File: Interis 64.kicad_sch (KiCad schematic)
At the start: 11 parts, among them J2 Ext. RESET, SW1 RESET, U1 DS1233, U2 Z80B CPU, Y1 7.3728MHz

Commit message: Memory expansion moved to low memory
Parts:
- J2: footprint Connector_PinHeader_2.54mm:PinHeader_1x02_P2.54mm_Vertical -> Connector_JST:JST_XH_B2B-XH-A_1x02_P2.50mm_Vertical
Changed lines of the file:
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@@
       (effects (font (size 1.27 1.27)) (justify left))
     )
-    (property "Footprint" "Connector_PinHeader_2.54mm:PinHeader_1x02_P2.54mm_Vertical" (at 111.125 41.91 0)
+    (property "Footprint" "Connector_JST:JST_XH_B2B-XH-A_1x02_P2.50mm_Vertical" (at 111.125 41.91 0)
       (effects (font (size 1.27 1.27)) hide)
     )

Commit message: Misc Updates/Cleanup
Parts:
- C29: value 0.01µF -> 0.1µF; footprint Capacitor_THT:C_Disc_D3.8mm_W2.6mm_P2.50mm -> Capacitor_THT:C_Disc_D5.0mm_W2.5mm_P2.50mm
- TP1, TP2: footprint TestPoint:TestPoint_THTPad_2.5x2.5mm_Drill1.2mm -> TestPoint:TestPoint_Loop_D2.60mm_Drill1.6mm_Beaded
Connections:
- net ~{RFSH}: now reaches U2.28 (~{RFSH})
- no-connect marks 2 -> 1
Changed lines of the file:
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@@
   )
   (no_connect (at 63.5 76.835))
-  (no_connect (at 133.35 112.395))
   (bus_entry (at 173.99 112.395) (size 2.54 -2.54)
     (stroke (width 0) (type default))
@@
   )
   (wire (pts (xy 127 38.1) (xy 127 84.455))
+    (stroke (width 0) (type default))
+  )
+  (wire (pts (xy 125.73 112.395) (xy 133.35 112.395))
     (stroke (width 0) (type default))
   )
@@
     (effects (font (size 1.27 1.27)) (justify right))
     (property "Intersheetrefs" "${INTERSHEET_REFS}" (at 86.2734 114.8556 0)
+      (effects (font (size 1.27 1.27)) (justify right) hide)
+    )
+  )
+  (global_label "~{RFSH}" (shape output) (at 125.73 112.395 180) (fields_autoplaced)
+    (effects (font (size 1.27 1.27)) (justify right))
+    (property "Intersheetrefs" "${INTERSHEET_REFS}" (at 118.1034 112.395 0)
       (effects (font (size 1.27 1.27)) (justify right) hide)
     )
@@
       (effects (font (size 1.27 1.27)) (justify right))
     )
-    (property "Value" "0.01µF" (at 80.645 44.45 0)
+    (property "Value" "0.1µF" (at 80.645 44.45 0)
       (effects (font (size 1.27 1.27)) (justify right))
     )
-    (property "Footprint" "Capacitor_THT:C_Disc_D3.8mm_W2.6mm_P2.50mm" (at 89.2048 46.99 0)
+    (property "Footprint" "Capacitor_THT:C_Disc_D5.0mm_W2.5mm_P2.50mm" (at 89.2048 46.99 0)
       (effects (font (size 1.27 1.27)) hide)
     )
@@
       (effects (font (size 1.27 1.27)) (justify right))
     )
-    (property "Footprint" "TestPoint:TestPoint_THTPad_2.5x2.5mm_Drill1.2mm" (at 121.92 33.02 0)
+    (property "Footprint" "TestPoint:TestPoint_Loop_D2.60mm_Drill1.6mm_Beaded" (at 121.92 33.02 0)
       (effects (font (size 1.27 1.27)) hide)
     )
@@
       (effects (font (size 1.27 1.27)))
     )
-    (property "Footprint" "TestPoint:TestPoint_THTPad_2.5x2.5mm_Drill1.2mm" (at 103.505 64.135 0)
-      (effects (font (size 1.27 1.27)) hide)
-    )
+    (property "Footprint" "TestPoint:TestPoint_Loop_D2.60mm_Drill1.6mm_Beaded" (at 103.505 64.135 0)
+      (effects (font (size 1.27 1.27)) hide)
+    )

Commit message: Work-in-progress
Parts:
- removed J2: Ext. RESET, Connector_JST:JST_XH_B2B-XH-A_1x02_P2.50mm_Vertical, symbol Connector_Generic:Conn_01x02
- removed SW1: RESET, Button_Switch_THT:SW_TH_Tactile_Omron_B3F-10xx, symbol Switch:SW_Push
- added J2: ExtReset, Connector_JST:JST_XH_B4B-XH-A_1x04_P2.50mm_Vertical, symbol Connector_Generic:Conn_01x04
- U1: footprint Package_TO_SOT_THT:TO-92_Inline -> Package_TO_SOT_THT:TO-92_HandSolder
- U2: footprint Package_DIP:DIP-40_W15.24mm_LongPads -> Package_DIP:DIP-40_W15.24mm
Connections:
- net +5V: now also J2.1 (Pin_1)
- net GND: now also J2.2 (Pin_2), J2.3 (Pin_3)
- net ~{RESET}: now also J2.4 (Pin_4)
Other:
- removed sheet PS2 Keyboard
- added sheet VT82C42 Input (VT82C42.kicad_sch)
- moved on the sheet: C29, TP2

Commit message: Work in progress
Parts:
- removed TP1: ~{RES}, TestPoint:TestPoint_Loop_D2.60mm_Drill1.6mm_Beaded, symbol Connector:TestPoint
- removed TP2: CLK, TestPoint:TestPoint_Loop_D2.60mm_Drill1.6mm_Beaded, symbol Connector:TestPoint
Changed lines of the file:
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@@
   (junction (at 37.465 135.89) (diameter 0) (color 0 0 0 0)
-  )
-  (junction (at 103.505 69.215) (diameter 0) (color 0 0 0 0)
   )
   (junction (at 97.79 38.1) (diameter 0) (color 0 0 0 0)
@@
   )
   (bus (pts (xy 176.53 130.175) (xy 176.53 132.715))
-    (stroke (width 0) (type default))
-  )
-  (wire (pts (xy 127 33.02) (xy 127 38.1))
     (stroke (width 0) (type default))
   )
@@
     )
   )
-  (symbol (lib_id "Connector:TestPoint") (at 127 33.02 0) (mirror y) (unit 1)
-    (in_bom yes) (on_board yes) (dnp no) (fields_autoplaced)
-    (property "Reference" "TP1" (at 128.397 28.7878 0)
-      (effects (font (size 1.27 1.27)) (justify right))
-    )
-    (property "Value" "~{RES}" (at 128.397 31.4787 0)
-      (effects (font (size 1.27 1.27)) (justify right))
-    )
-    (property "Footprint" "TestPoint:TestPoint_Loop_D2.60mm_Drill1.6mm_Beaded" (at 121.92 33.02 0)
-      (effects (font (size 1.27 1.27)) hide)
-    )
-    (property "Datasheet" "~" (at 121.92 33.02 0)
-      (effects (font (size 1.27 1.27)) hide)
-    )
-    (pin "1")
-    (instances
-      (project "Interis 64"
-        (path "/b7aa0362-7c9e-4a42-b191-ab15a38bf3c5"
-          (reference "TP1") (unit 1)
-        )
-      )
-    )
-  )
   (symbol (lib_id "power:GND") (at 71.12 85.725 0) (unit 1)
     (in_bom yes) (on_board yes) (dnp no)
@@
         )
       )
-    )
-  )
-  (symbol (lib_id "Connector:TestPoint") (at 103.505 69.215 0) (unit 1)
-    (in_bom yes) (on_board yes) (dnp no) (fields_autoplaced)
-    (property "Reference" "TP2" (at 104.902 65.2693 0)
-      (effects (font (size 1.27 1.27)) (justify left))
-    )
-    (property "Value" "CLK" (at 104.902 67.1903 0)
-      (effects (font (size 1.27 1.27)) (justify left))
-    )
-    (property "Footprint" "TestPoint:TestPoint_Loop_D2.60mm_Drill1.6mm_Beaded" (at 108.585 69.215 0)
-      (effects (font (size 1.27 1.27)) hide)
-    )
-    (property "Datasheet" "~" (at 108.585 69.215 0)
-      (effects (font (size 1.27 1.27)) hide)
-    )
-    (pin "1")
-    (instances
-      (project "Interis 64"
-        (path "/b7aa0362-7c9e-4a42-b191-ab15a38bf3c5"
-          (reference "TP2") (unit 1)
-        )
-      )

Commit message: Layout Tweaks
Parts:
- added J1: PwrLED, Connector_PinHeader_2.54mm:PinHeader_1x02_P2.54mm_Vertical, symbol Connector_Generic:Conn_01x02
- J2: footprint Connector_JST:JST_XH_B4B-XH-A_1x04_P2.50mm_Vertical -> Connector_PinHeader_2.54mm:PinHeader_1x02_P2.54mm_Vertical; symbol Connector_Generic:Conn_01x04 -> Connector_Generic:Conn_01x02
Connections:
- net +5V: now also J1.2 (Pin_2); no longer J2.1 (Pin_1)
- net GND: now also J2.1 (Pin_1), J1.1 (Pin_1); no longer J2.2 (Pin_2), J2.3 (Pin_3)
- net ~{RESET}: now also J2.2 (Pin_2); no longer J2.4 (Pin_4)
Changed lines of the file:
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@@
   (junction (at 103.505 99.695) (diameter 0) (color 0 0 0 0)
-  )
-  (junction (at 37.465 135.89) (diameter 0) (color 0 0 0 0)
   )
   (junction (at 97.79 38.1) (diameter 0) (color 0 0 0 0)
@@
     (stroke (width 0) (type default))
   )
+  (wire (pts (xy 48.895 160.02) (xy 52.705 160.02))
+    (stroke (width 0) (type default))
+  )
   (wire (pts (xy 168.91 112.395) (xy 173.99 112.395))
     (stroke (width 0) (type default))
@@
     (stroke (width 0) (type default))
   )
+  (wire (pts (xy 37.465 162.56) (xy 52.705 162.56))
+    (stroke (width 0) (type default))
+  )
   (wire (pts (xy 168.91 140.335) (xy 173.99 140.335))
     (stroke (width 0) (type default))
@@
     (stroke (width 0) (type default))
   )
-  (wire (pts (xy 37.465 135.89) (xy 37.465 144.78))
+  (wire (pts (xy 37.465 133.35) (xy 37.465 144.78))
     (stroke (width 0) (type default))
   )
@@
     (stroke (width 0) (type default))
   )
+  (wire (pts (xy 48.895 156.845) (xy 48.895 160.02))
+    (stroke (width 0) (type default))
+  )
   (wire (pts (xy 168.91 120.015) (xy 173.99 120.015))
     (stroke (width 0) (type default))
@@
     (stroke (width 0) (type default))
   )
-  (wire (pts (xy 37.465 133.35) (xy 37.465 135.89))
-    (stroke (width 0) (type default))
-  )
   (bus (pts (xy 176.53 78.105) (xy 182.88 78.105))
     (stroke (width 0) (type default))
@@
     (stroke (width 0) (type default))
   )
-  (wire (pts (xy 48.895 130.81) (xy 52.705 130.81))
-    (stroke (width 0) (type default))
-  )
   (wire (pts (xy 92.71 142.875) (xy 103.505 142.875))
     (stroke (width 0) (type default))
@@
     (stroke (width 0) (type default))
   )
-  (wire (pts (xy 48.895 127.635) (xy 48.895 130.81))
-    (stroke (width 0) (type default))
-  )
   (bus (pts (xy 176.53 92.075) (xy 176.53 94.615))
     (stroke (width 0) (type default))
@@
     (stroke (width 0) (type default))
   )
+  (wire (pts (xy 37.465 162.56) (xy 37.465 173.99))
+    (stroke (width 0) (type default))
+  )
   (wire (pts (xy 125.73 132.715) (xy 133.35 132.715))
     (stroke (width 0) (type default))
@@
   )
   (bus (pts (xy 176.53 97.155) (xy 176.53 99.695))
-    (stroke (width 0) (type default))
-  )
-  (wire (pts (xy 37.465 135.89) (xy 52.705 135.89))
     (stroke (width 0) (type default))
   )
@@
     )
   )
-  (global_label "~{RESET}" (shape bidirectional) (at 52.705 138.43 180) (fields_autoplaced)
-    (effects (font (size 1.27 1.27)) (justify right))
-    (property "Intersheetrefs" "${INTERSHEET_REFS}" (at 44.6356 138.3506 0)
+  (global_label "~{RESET}" (shape bidirectional) (at 52.705 135.89 180) (fields_autoplaced)
+    (effects (font (size 1.27 1.27)) (justify right))
+    (property "Intersheetrefs" "${INTERSHEET_REFS}" (at 44.6356 135.8106 0)
       (effects (font (size 1.27 1.27)) (justify right) hide)
     )
@@
     )
   )
+  (symbol (lib_id "power:GND") (at 37.465 173.99 0) (unit 1)
+    (in_bom yes) (on_board yes) (dnp no)
+    (property "Reference" "#PWR080" (at 37.465 180.34 0)
+      (effects (font (size 1.27 1.27)) hide)
+    )
+    (property "Value" "GND" (at 37.592 178.3842 0)
+      (effects (font (size 1.27 1.27)))
+    )
+    (property "Footprint" "" (at 37.465 173.99 0)
+      (effects (font (size 1.27 1.27)) hide)
+    )
+    (property "Datasheet" "" (at 37.465 173.99 0)
+      (effects (font (size 1.27 1.27)) hide)
+    )
+    (pin "1")
+    (instances
+      (project "Interis 64"
+        (path "/b7aa0362-7c9e-4a42-b191-ab15a38bf3c5"
+          (reference "#PWR080") (unit 1)
+        )
+      )
+    )
+  )
   (symbol (lib_id "Device:C") (at 97.79 43.18 0) (mirror y) (unit 1)
     (in_bom yes) (on_board yes) (dnp no)
@@
     )
   )
-  (symbol (lib_id "Connector_Generic:Conn_01x04") (at 57.785 133.35 0) (unit 1)
+  (symbol (lib_id "Connector_Generic:Conn_01x02") (at 57.785 133.35 0) (unit 1)
     (in_bom yes) (on_board yes) (dnp no) (fields_autoplaced)
     (property "Reference" "J2" (at 59.817 133.9763 0)
@@
       (effects (font (size 1.27 1.27)) (justify left))
     )
-    (property "Footprint" "Connector_JST:JST_XH_B4B-XH-A_1x04_P2.50mm_Vertical" (at 57.785 133.35 0)
+    (property "Footprint" "Connector_PinHeader_2.54mm:PinHeader_1x02_P2.54mm_Vertical" (at 57.785 133.35 0)
       (effects (font (size 1.27 1.27)) hide)
     )
@@
     (pin "1")
     (pin "2")
-    (pin "3")
-    (pin "4")
     (instances
       (project "Interis 64"
@@
     )
   )
-  (symbol (lib_id "power:+5V") (at 48.895 127.635 0) (unit 1)
-    (in_bom yes) (on_board yes) (dnp no)
-    (property "Reference" "#PWR022" (at 48.895 131.445 0)
-      (effects (font (size 1.27 1.27)) hide)
-    )
-    (property "Value" "+5V" (at 49.276 123.2408 0)
-      (effects (font (size 1.27 1.27)))
-    )
-    (property "Footprint" "" (at 48.895 127.635 0)
-      (effects (font (size 1.27 1.27)) hide)
-    )
-    (property "Datasheet" "" (at 48.895 127.635 0)
-      (effects (font (size 1.27 1.27)) hide)
-    )
-    (pin "1")
-    (instances
-      (project "Interis 64"
-        (path "/b7aa0362-7c9e-4a42-b191-ab15a38bf3c5"
-          (reference "#PWR022") (unit 1)
+  (symbol (lib_id "power:+5V") (at 48.895 156.845 0) (unit 1)
+    (in_bom yes) (on_board yes) (dnp no)
+    (property "Reference" "#PWR024" (at 48.895 160.655 0)
+      (effects (font (size 1.27 1.27)) hide)
+    )
+    (property "Value" "+5V" (at 49.276 152.4508 0)
+      (effects (font (size 1.27 1.27)))
+    )
+    (property "Footprint" "" (at 48.895 156.845 0)
+      (effects (font (size 1.27 1.27)) hide)
+    )
+    (property "Datasheet" "" (at 48.895 156.845 0)
+      (effects (font (size 1.27 1.27)) hide)
+    )
+    (pin "1")
+    (instances
+      (project "Interis 64"
+        (path "/b7aa0362-7c9e-4a42-b191-ab15a38bf3c5"
+          (reference "#PWR024") (unit 1)
         )
       )
@@
         )
       )
+    )
+  )
+  (symbol (lib_id "Connector_Generic:Conn_01x02") (at 57.785 162.56 0) (mirror x) (unit 1)
+    (in_bom yes) (on_board yes) (dnp no)
+    (property "Reference" "J1" (at 59.817 163.2037 0)
+      (effects (font (size 1.27 1.27)) (justify left))
+    )
+    (property "Value" "PwrLED" (at 59.817 161.2827 0)
+      (effects (font (size 1.27 1.27)) (justify left))
+    )
+    (property "Footprint" "Connector_PinHeader_2.54mm:PinHeader_1x02_P2.54mm_Vertical" (at 57.785 162.56 0)
+      (effects (font (size 1.27 1.27)) hide)
+    )
+    (property "Datasheet" "~" (at 57.785 162.56 0)
+      (effects (font (size 1.27 1.27)) hide)
+    )
+    (pin "1")
+    (pin "2")
+    (instances
+      (project "Interis 64"
+        (path "/b7aa0362-7c9e-4a42-b191-ab15a38bf3c5"
+          (reference "J1") (unit 1)
+        )
+      )

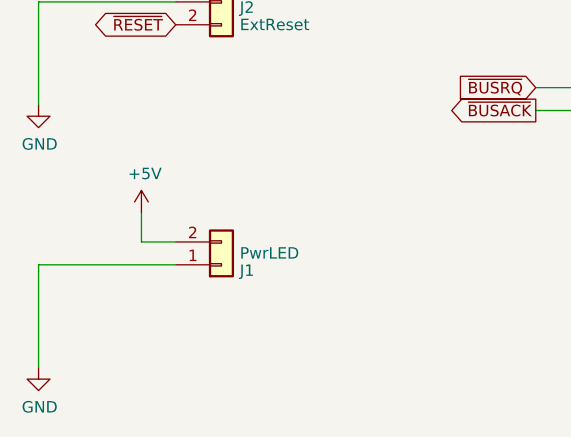
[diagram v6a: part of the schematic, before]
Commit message: Add CC lines
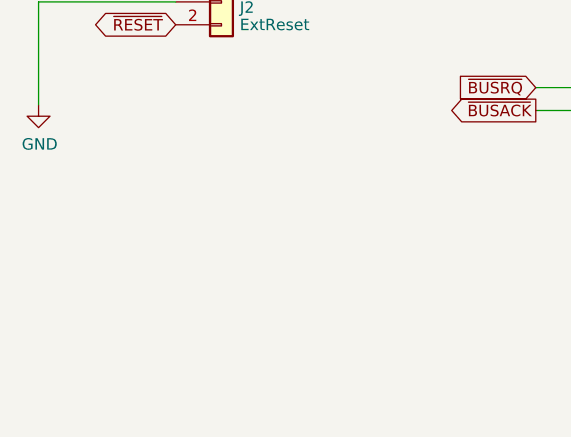
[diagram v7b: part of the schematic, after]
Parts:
- removed J1: PwrLED, Connector_PinHeader_2.54mm:PinHeader_1x02_P2.54mm_Vertical, symbol Connector_Generic:Conn_01x02
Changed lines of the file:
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@@
-    (stroke (width 0) (type default))
-  )
-  (wire (pts (xy 48.895 160.02) (xy 52.705 160.02))
     (stroke (width 0) (type default))
   )
@@
     (stroke (width 0) (type default))
   )
-  (wire (pts (xy 37.465 162.56) (xy 52.705 162.56))
-    (stroke (width 0) (type default))
-  )
   (wire (pts (xy 168.91 140.335) (xy 173.99 140.335))
     (stroke (width 0) (type default))
@@
     (stroke (width 0) (type default))
   )
-  (wire (pts (xy 48.895 156.845) (xy 48.895 160.02))
-    (stroke (width 0) (type default))
-  )
   (wire (pts (xy 168.91 120.015) (xy 173.99 120.015))
     (stroke (width 0) (type default))
@@
   )
   (bus (pts (xy 176.53 84.455) (xy 176.53 86.995))
-    (stroke (width 0) (type default))
-  )
-  (wire (pts (xy 37.465 162.56) (xy 37.465 173.99))
     (stroke (width 0) (type default))
   )
@@
     )
   )
-  (symbol (lib_id "power:GND") (at 37.465 173.99 0) (unit 1)
-    (in_bom yes) (on_board yes) (dnp no)
-    (property "Reference" "#PWR080" (at 37.465 180.34 0)
-      (effects (font (size 1.27 1.27)) hide)
-    )
-    (property "Value" "GND" (at 37.592 178.3842 0)
-      (effects (font (size 1.27 1.27)))
-    )
-    (property "Footprint" "" (at 37.465 173.99 0)
-      (effects (font (size 1.27 1.27)) hide)
-    )
-    (property "Datasheet" "" (at 37.465 173.99 0)
-      (effects (font (size 1.27 1.27)) hide)
-    )
-    (pin "1")
-    (instances
-      (project "Interis 64"
-        (path "/b7aa0362-7c9e-4a42-b191-ab15a38bf3c5"
-          (reference "#PWR080") (unit 1)
-        )
-      )
-    )
-  )
   (symbol (lib_id "Device:C") (at 97.79 43.18 0) (mirror y) (unit 1)
     (in_bom yes) (on_board yes) (dnp no)
@@
     )
   )
-  (symbol (lib_id "power:+5V") (at 48.895 156.845 0) (unit 1)
-    (in_bom yes) (on_board yes) (dnp no)
-    (property "Reference" "#PWR024" (at 48.895 160.655 0)
-      (effects (font (size 1.27 1.27)) hide)
-    )
-    (property "Value" "+5V" (at 49.276 152.4508 0)
-      (effects (font (size 1.27 1.27)))
-    )
-    (property "Footprint" "" (at 48.895 156.845 0)
-      (effects (font (size 1.27 1.27)) hide)
-    )
-    (property "Datasheet" "" (at 48.895 156.845 0)
-      (effects (font (size 1.27 1.27)) hide)
-    )
-    (pin "1")
-    (instances
-      (project "Interis 64"
-        (path "/b7aa0362-7c9e-4a42-b191-ab15a38bf3c5"
-          (reference "#PWR024") (unit 1)
-        )
-      )
-    )
-  )
   (symbol (lib_id "Device:R_US") (at 103.505 137.795 180) (unit 1)
     (in_bom yes) (on_board yes) (dnp no) (fields_autoplaced)
@@
         )
       )
-    )
-  )
-  (symbol (lib_id "Connector_Generic:Conn_01x02") (at 57.785 162.56 0) (mirror x) (unit 1)
-    (in_bom yes) (on_board yes) (dnp no)
-    (property "Reference" "J1" (at 59.817 163.2037 0)
-      (effects (font (size 1.27 1.27)) (justify left))
-    )
-    (property "Value" "PwrLED" (at 59.817 161.2827 0)
-      (effects (font (size 1.27 1.27)) (justify left))
-    )
-    (property "Footprint" "Connector_PinHeader_2.54mm:PinHeader_1x02_P2.54mm_Vertical" (at 57.785 162.56 0)
-      (effects (font (size 1.27 1.27)) hide)
-    )
-    (property "Datasheet" "~" (at 57.785 162.56 0)
-      (effects (font (size 1.27 1.27)) hide)
-    )
-    (pin "1")
-    (pin "2")
-    (instances
-      (project "Interis 64"
-        (path "/b7aa0362-7c9e-4a42-b191-ab15a38bf3c5"
-          (reference "J1") (unit 1)
-        )
-      )
